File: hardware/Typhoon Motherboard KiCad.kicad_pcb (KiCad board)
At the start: 2 copper layers, 8 parts, among them J1 Conn_01x04_Pin, J2 Conn_02x03_Odd_Even, U1 ESP32-S3-WROOM-1, U2 AZ1117-3.3

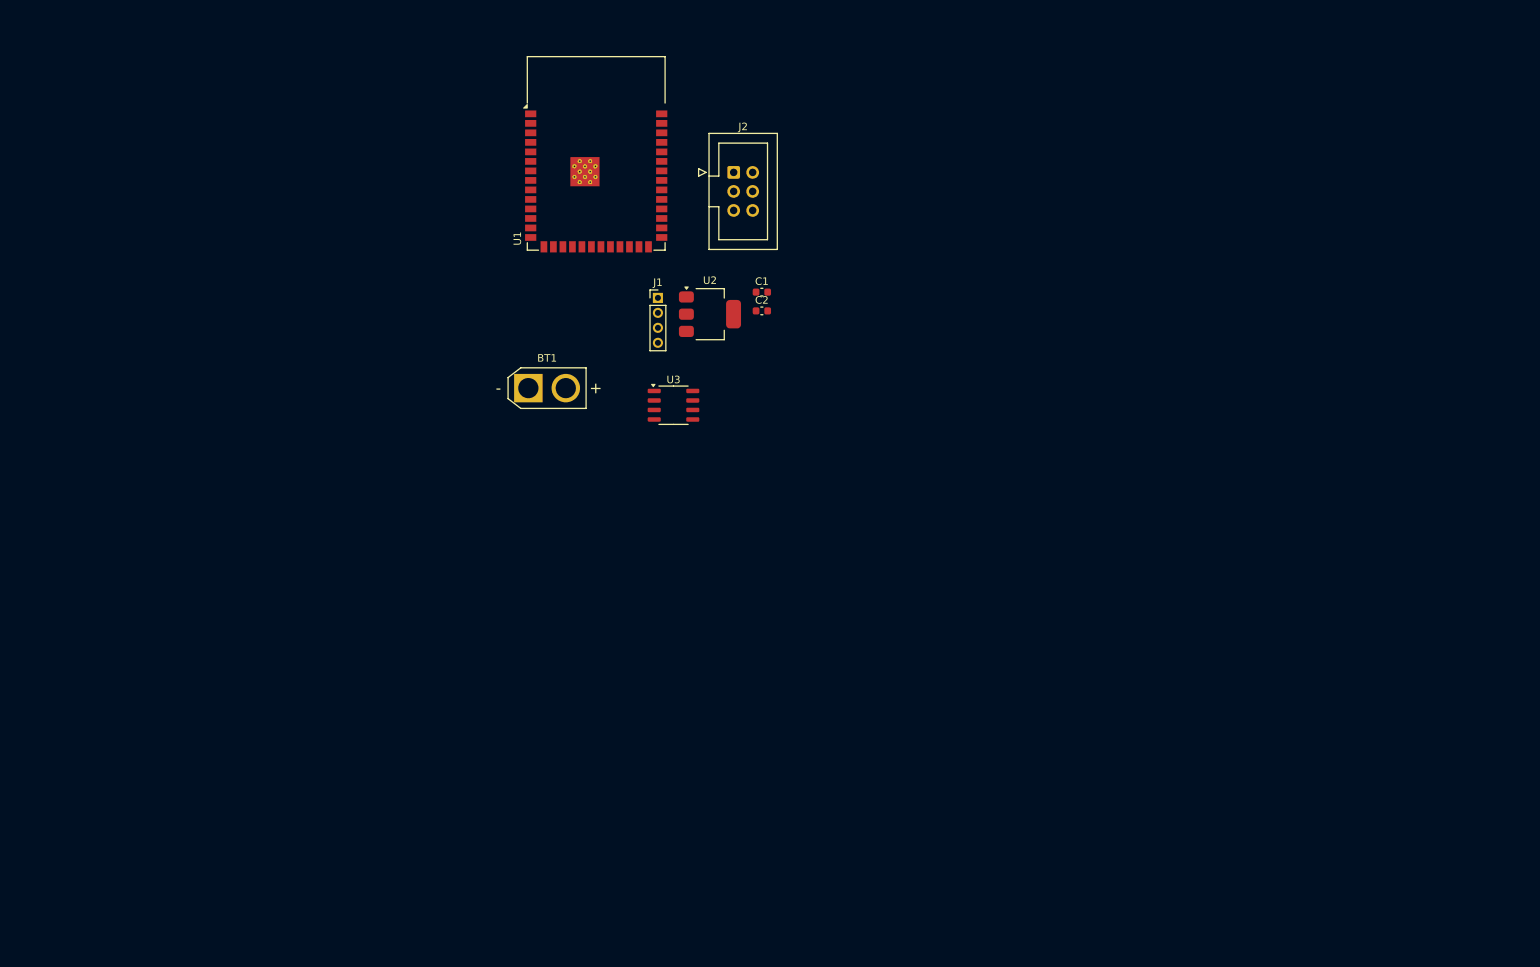
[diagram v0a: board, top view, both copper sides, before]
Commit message: Update Schematics and Start PCB
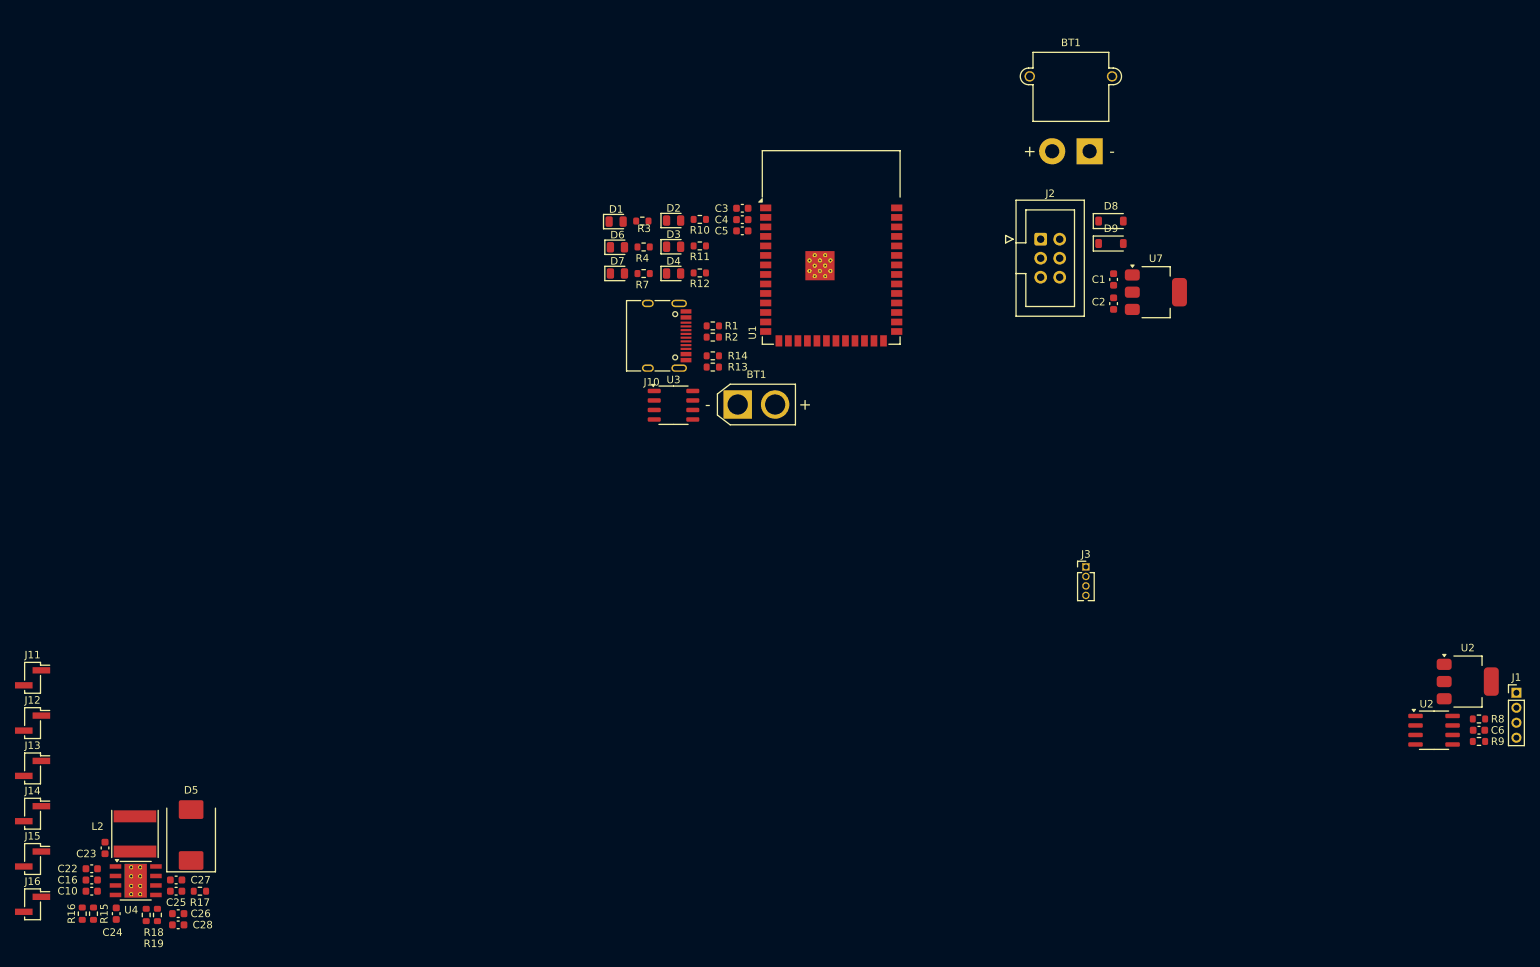
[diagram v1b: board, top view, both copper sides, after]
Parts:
- added BT1: XT30, Connector_AMASS:AMASS_XT30PW-M_1x02_P2.50mm_Horizontal, F.Cu at (176.0, 73.2)
- added C10: 4.7u, Capacitor_SMD:C_0603_1608Metric, F.Cu at (42.7, 172.0)
- added C16: 4.7u, Capacitor_SMD:C_0603_1608Metric, F.Cu at (42.7, 170.5)
- added C22: 4.7u, Capacitor_SMD:C_0603_1608Metric, F.Cu at (42.7, 169.0)
- added C23: 0.1u, Capacitor_SMD:C_0603_1608Metric, F.Cu at (44.5, 166.2)
- added C24: 0.01u, Capacitor_SMD:C_0603_1608Metric, F.Cu at (46.0, 175.0)
- added C25: 1000p, Capacitor_SMD:C_0603_1608Metric, F.Cu at (54.0, 172.0)
- added C26: 47u, Capacitor_SMD:C_0603_1608Metric, F.Cu at (54.3, 175.0)
- added C27: 47u, Capacitor_SMD:C_0603_1608Metric, F.Cu at (54.0, 170.5)
- added C28: 47u, Capacitor_SMD:C_0603_1608Metric, F.Cu at (54.3, 176.5)
- added C3: 10u, Capacitor_SMD:C_0603_1608Metric, F.Cu at (129.6, 80.8)
- added C4: 1u, Capacitor_SMD:C_0603_1608Metric, F.Cu at (129.6, 82.3)
- added C5: 0.1u, Capacitor_SMD:C_0603_1608Metric, F.Cu at (129.6, 83.8)
- added C6: 4.7n, Capacitor_SMD:C_0603_1608Metric, F.Cu at (228.0, 150.5)
- added D1: LED, LED_SMD:LED_0805_2012Metric, F.Cu at (112.8, 82.6)
- added D2: LED, LED_SMD:LED_0805_2012Metric, F.Cu at (120.4, 82.4)
- added D3: LED, LED_SMD:LED_0805_2012Metric, F.Cu at (120.4, 85.9)
- added D4: LED, LED_SMD:LED_0805_2012Metric, F.Cu at (120.4, 89.5)
- added D5: B340, Diode_SMD:D_SMC, F.Cu at (56.0, 164.5)
- added D6: LED, LED_SMD:LED_0805_2012Metric, F.Cu at (112.9, 86.0)
- added D7: LED, LED_SMD:LED_0805_2012Metric, F.Cu at (112.9, 89.5)
- added D8: D, Diode_SMD:D_SOD-123, F.Cu at (178.8, 82.5)
- added D9: D, Diode_SMD:D_SOD-123, F.Cu at (178.8, 85.5)
- added J10: USB_C_Receptacle_USB2.0, Connector_USB:USB_C_Receptacle_HRO_TYPE-C-31-M-12, F.Cu at (118.0, 97.8)
- added J11: Conn_01x02_Pin, Connector_PinHeader_2.00mm:PinHeader_1x02_P2.00mm_Vertical_SMD_Pin1Right, F.Cu at (34.8, 143.5)
- added J12: Conn_01x02_Pin, Connector_PinHeader_2.00mm:PinHeader_1x02_P2.00mm_Vertical_SMD_Pin1Right, F.Cu at (34.8, 149.6)
- added J13: Conn_01x02_Pin, Connector_PinHeader_2.00mm:PinHeader_1x02_P2.00mm_Vertical_SMD_Pin1Right, F.Cu at (34.8, 155.6)
- added J14: Conn_01x02_Pin, Connector_PinHeader_2.00mm:PinHeader_1x02_P2.00mm_Vertical_SMD_Pin1Right, F.Cu at (34.8, 161.7)
- added J15: Conn_01x02_Pin, Connector_PinHeader_2.00mm:PinHeader_1x02_P2.00mm_Vertical_SMD_Pin1Right, F.Cu at (34.8, 167.7)
- added J16: Conn_01x02_Pin, Connector_PinHeader_2.00mm:PinHeader_1x02_P2.00mm_Vertical_SMD_Pin1Right, F.Cu at (34.8, 173.8)
- added J3: Conn_01x04_Pin, Connector_PinHeader_1.27mm:PinHeader_1x04_P1.27mm_Vertical, F.Cu at (175.5, 128.7)
- added L2: 4.7u, Inductor_SMD:L_Taiyo-Yuden_NR-60xx, F.Cu at (48.5, 164.3)
- added R1: 22R, Resistor_SMD:R_0603_1608Metric, F.Cu at (125.7, 96.5)
- added R10: 320, Resistor_SMD:R_0603_1608Metric, F.Cu at (123.9, 82.3)
- added R11: 320, Resistor_SMD:R_0603_1608Metric, F.Cu at (123.9, 85.8)
- added R12: 320, Resistor_SMD:R_0603_1608Metric, F.Cu at (123.9, 89.4)
- added R13: 5.1K, Resistor_SMD:R_0603_1608Metric, F.Cu at (125.7, 102.0)
- added R14: 5.1K, Resistor_SMD:R_0603_1608Metric, F.Cu at (125.7, 100.5)
- added R15: 200k, Resistor_SMD:R_0603_1608Metric, F.Cu at (43.0, 175.0)
- added R16: 98k, Resistor_SMD:R_0603_1608Metric, F.Cu at (41.5, 175.0)
- added R17: 29.4k, Resistor_SMD:R_0603_1608Metric, F.Cu at (57.2, 172.0)
- added R18: 10.2k, Resistor_SMD:R_0603_1608Metric, F.Cu at (50.0, 175.2)
- added R19: 3.24k, Resistor_SMD:R_0603_1608Metric, F.Cu at (51.5, 175.2)
- added R2: 22R, Resistor_SMD:R_0603_1608Metric, F.Cu at (125.7, 98.0)
- added R3: 320, Resistor_SMD:R_0603_1608Metric, F.Cu at (116.3, 82.5)
- added R4: 320, Resistor_SMD:R_0603_1608Metric, F.Cu at (116.4, 86.0)
- added R7: 320, Resistor_SMD:R_0603_1608Metric, F.Cu at (116.4, 89.5)
- added R8: 60, Resistor_SMD:R_0603_1608Metric, F.Cu at (228.0, 149.0)
- added R9: 60, Resistor_SMD:R_0603_1608Metric, F.Cu at (228.0, 152.0)
- added U2: SN65HVD233, Package_SO:SOIC-8_3.9x4.9mm_P1.27mm, F.Cu at (222.0, 150.5)
- added U4: TPS54331DDA, Package_SO:TI_SO-PowerPAD-8_ThermalVias, F.Cu at (48.6, 170.6)
- added U7: MCP1825S, Package_TO_SOT_SMD:SOT-223-3_TabPin2, F.Cu at (184.8, 92.0)
- moved J1 126.2 mm to (233.0, 145.5)
- moved U2 112.5 mm to (226.5, 144.0)
- moved C1 47.0 mm to (179.2, 90.3), turned to 90 degrees
- moved C2 47.0 mm to (179.2, 93.5), turned to -90 degrees
- moved J2 42.0 mm to (169.5, 84.9)
- moved U1 33.8 mm to (141.5, 86.0)
- moved BT1 28.0 mm to (129.0, 107.0)
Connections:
- J1 pad 1: +3V3 -> GND
- J1 pad 2: GND -> +3.3V
- J1 pad 3: /CANH -> /CAN_{H}
- J1 pad 4: /CANL -> /CAN_{L}
- J2 pad 2: +3V3 -> +3.3V
- J2 pad 3: /TX -> /Prog/TypeC_{TX}
- J2 pad 5: /RX -> /Prog/TypeC_{RX}
- U1 pad 10: unconnected-(U1-IO17-Pad10) -> /Mother_{TX}
- U1 pad 11: unconnected-(U1-IO18-Pad11) -> /Mother_{RX}
- U1 pad 12: unconnected-(U1-IO8-Pad12) -> /LED_{4}
- U1 pad 13: Net-(U1-IO19) -> /D-
- U1 pad 14: Net-(U1-IO20) -> /D+
- U1 pad 2: +3V3 -> +3.3V
- U1 pad 36: /RX -> /Prog/TypeC_{RX}
- U1 pad 37: /TX -> /Prog/TypeC_{TX}
- U1 pad 5: unconnected-(U1-IO5-Pad5) -> /LED_{1}
- U1 pad 6: unconnected-(U1-IO6-Pad6) -> /LED_{2}
- U1 pad 7: unconnected-(U1-IO7-Pad7) -> /LED_{3}
- U1 pad 8: unconnected-(U1-IO15-Pad8) -> /LED_{5}
- U1 pad 9: unconnected-(U1-IO16-Pad9) -> /LED_{6}

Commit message: First draft of PCB
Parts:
- removed the BT1 at (129.0, 107.0)
- removed the U2 at (226.5, 144.0)
- removed the U2 at (222.0, 150.5)
- removed U3: ~, Package_SO:SO-8_3.9x4.9mm_P1.27mm
- added U2: SN65HVD233, Package_SO:SOIC-8_3.9x4.9mm_P1.27mm, F.Cu at (157.5, 103.6)
- moved J16 133.1 mm to (157.2, 121.3), turned to 90 degrees
- moved J15 125.2 mm to (151.2, 121.3), turned to 90 degrees
- moved C23 122.5 mm to (154.5, 112.2)
- moved L2 121.4 mm to (159.0, 114.0)
- moved D5 120.9 mm to (166.0, 114.5)
- moved J14 117.4 mm to (145.1, 121.3), turned to 90 degrees
- moved R17 114.1 mm to (150.7, 106.7)
- moved R18 114.1 mm to (143.5, 109.8)
- moved R19 114.1 mm to (145.0, 109.8)
- moved C10 114.1 mm to (136.3, 106.7)
- moved C16 114.1 mm to (136.3, 105.2)
- moved C22 114.1 mm to (136.3, 103.7)
- moved C24 114.1 mm to (139.5, 109.7)
- moved C25 114.1 mm to (147.5, 106.7)
- moved C26 114.1 mm to (147.8, 109.7)
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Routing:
- net +3.3V: track 0.00 -> 74.7 mm, vias 0 -> 3
- net /Prog/TypeC_{RX}: track 0.00 -> 57.1 mm
- net +5V: track 0.00 -> 37.6 mm
- net /EN: track 0.00 -> 33.5 mm, vias 0 -> 1
- net /Prog/TypeC_{TX}: track 0.00 -> 32.3 mm
- net /LED_{6}: track 0.00 -> 30.5 mm, vias 0 -> 2
- net /LED_{5}: track 0.00 -> 29.6 mm, vias 0 -> 2
- net /LED_{4}: track 0.00 -> 29.1 mm, vias 0 -> 2
- net Net-(D5-K): track 0.00 -> 29.1 mm, vias 0 -> 2
- net +BATT: track 0.00 -> 28.8 mm
- net VDC: track 0.00 -> 28.1 mm
- net /LED_{3}: track 0.00 -> 27.5 mm, vias 0 -> 2
- net /LED_{2}: track 0.00 -> 26.9 mm, vias 0 -> 2
- net /Mother_{RX}: track 0.00 -> 26.2 mm
- net /LED_{1}: track 0.00 -> 26.2 mm, vias 0 -> 2
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- added copper zone on F.Cu, net +3.3V
- added copper zone on F.Cu, net +3.3VA
- added copper zone on B.Cu, net GND
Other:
- board outline added: 67.5 x 73 mm

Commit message: Finalized First Draft of the PCB
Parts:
- moved U2 0.60 mm to (158.0, 103.8)
- turned D8 to 180 degrees
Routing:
- net Net-(J10-CC1): track 12.4 -> 8.34 mm, vias 0 -> 2
- net +3.3V: track 74.7 -> 78.7 mm
- net /Prog/TypeC_{RX}: track 57.1 -> 54.8 mm
- net Net-(D2-A): track 0.00 -> 1.80 mm
- net Net-(D3-A): track 0.00 -> 1.78 mm
- net Net-(D4-A): track 0.00 -> 1.77 mm
- net Net-(D1-A): track 0.00 -> 1.77 mm
- net Net-(D6-A): track 0.00 -> 1.75 mm
- net Net-(D7-A): track 0.00 -> 1.74 mm
- net +5V: track 37.6 -> 39.3 mm
- net /D-: track 24.9 -> 26.6 mm
- net /D+: track 24.0 -> 25.7 mm
- net +BATT: track 28.8 -> 30.4 mm
- net /Prog/TypeC_{TX}: track 32.3 -> 33.7 mm
- net GND: vias 37 -> 39

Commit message: Fixed Placement issues (aesthetic fixes)
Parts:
- moved J3 47.3 mm to (112.7, 120.2), turned to 90 degrees
- moved J10 0.93 mm to (112.0, 85.2)
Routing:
- net +3.3V: track 78.7 -> 141.7 mm
- net /Mother_{TX}: track 26.0 -> 38.9 mm, vias 0 -> 2
- net /Mother_{RX}: track 26.2 -> 38.0 mm, vias 0 -> 2
- net /D+: track 25.7 -> 24.8 mm
- net Net-(J10-CC1): track 8.34 -> 9.06 mm
- net VDC: track 28.1 -> 27.6 mm

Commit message: Update (Round Edges)
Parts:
- moved J11 0.65 mm to (127.0, 120.7)
- moved J12 0.65 mm to (133.0, 120.7)
- moved J13 0.65 mm to (139.1, 120.7)
- moved J14 0.65 mm to (145.1, 120.7)
- moved J15 0.65 mm to (151.2, 120.7)
- moved J16 0.65 mm to (157.2, 120.7)
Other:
- board size 67.5 x 73 mm -> 65.7 x 44.9 mm
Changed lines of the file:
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@@
 		(tags "usb usb-c 2.0 pd")
 		(property "Reference" "J10"
-			(at -6.82 1.05 180)
+			(at -0.75 4.8 -90)
 			(layer "F.SilkS")
 			(effects
@@
 	(footprint "Connector_PinHeader_2.00mm:PinHeader_1x02_P2.00mm_Vertical_SMD_Pin1Right"
 		(layer "F.Cu")
-		(at 133 121.325 90)
+		(at 133 120.675 90)
 		(descr "surface-mounted straight pin header, 1x02, 2.00mm pitch, single row, style 2 (pin 1 right)")
 		(tags "Surface mounted pin header SMD 1x02 2.00mm single row style2 pin1 right")
 		(property "Reference" "J12"
-			(at 0 -3.06 270)
+			(at -2.075 -1 0)
 			(layer "F.SilkS")
 			(effects
@@
 	(footprint "Connector_PinHeader_2.00mm:PinHeader_1x02_P2.00mm_Vertical_SMD_Pin1Right"
 		(layer "F.Cu")
-		(at 126.95 121.325 90)
+		(at 126.95 120.675 90)
 		(descr "surface-mounted straight pin header, 1x02, 2.00mm pitch, single row, style 2 (pin 1 right)")
 		(tags "Surface mounted pin header SMD 1x02 2.00mm single row style2 pin1 right")
 		(property "Reference" "J11"
-			(at 0 -3.06 270)
+			(at -2.075 -0.95 0)
 			(layer "F.SilkS")
 			(effects
@@
 	(footprint "Connector_PinHeader_2.00mm:PinHeader_1x02_P2.00mm_Vertical_SMD_Pin1Right"
 		(layer "F.Cu")
-		(at 157.2 121.325 90)
+		(at 157.2 120.675 90)
 		(descr "surface-mounted straight pin header, 1x02, 2.00mm pitch, single row, style 2 (pin 1 right)")
 		(tags "Surface mounted pin header SMD 1x02 2.00mm single row style2 pin1 right")
 		(property "Reference" "J16"
-			(at 0 -3.06 270)
+			(at -2.075 -0.95 0)
 			(layer "F.SilkS")
 			(effects
@@
 	(footprint "Connector_PinHeader_2.00mm:PinHeader_1x02_P2.00mm_Vertical_SMD_Pin1Right"
 		(layer "F.Cu")
-		(at 151.15 121.325 90)
+		(at 151.15 120.675 90)
 		(descr "surface-mounted straight pin header, 1x02, 2.00mm pitch, single row, style 2 (pin 1 right)")
 		(tags "Surface mounted pin header SMD 1x02 2.00mm single row style2 pin1 right")
 		(property "Reference" "J15"
-			(at 0 -3.06 270)
+			(at -2.075 -0.9 0)
 			(layer "F.SilkS")
 			(effects
@@
 	(footprint "Connector_PinHeader_2.00mm:PinHeader_1x02_P2.00mm_Vertical_SMD_Pin1Right"
 		(layer "F.Cu")
-		(at 145.1 121.325 90)
+		(at 145.1 120.675 90)
 		(descr "surface-mounted straight pin header, 1x02, 2.00mm pitch, single row, style 2 (pin 1 right)")
 		(tags "Surface mounted pin header SMD 1x02 2.00mm single row style2 pin1 right")
 		(property "Reference" "J14"
-			(at 0 -3.06 270)
+			(at -2.075 -0.85 0)
 			(layer "F.SilkS")
 			(effects
@@
 	(footprint "Connector_PinHeader_2.00mm:PinHeader_1x02_P2.00mm_Vertical_SMD_Pin1Right"
 		(layer "F.Cu")
-		(at 139.05 121.325 90)
+		(at 139.05 120.675 90)
 		(descr "surface-mounted straight pin header, 1x02, 2.00mm pitch, single row, style 2 (pin 1 right)")
 		(tags "Surface mounted pin header SMD 1x02 2.00mm single row style2 pin1 right")
 		(property "Reference" "J13"
-			(at 0 -3.06 270)
+			(at -2.075 -0.8 0)
 			(layer "F.SilkS")
 			(effects
@@
 	)
 	(gr_line
-		(start 173 128)
-		(end 173 55)
+		(start 171.25 123)
+		(end 171.18934 81.06066)
 		(stroke
 			(width 0.05)
@@
 	)
 	(gr_line
-		(start 105.5 55)
-		(end 105.5 128)
+		(start 105.56066 81.06066)
+		(end 105.56066 122.93934)
+		(stroke
+			(width 0.05)
+			(type default)
+		)
+		(layer "Edge.Cuts")
+	)
+	(gr_arc
+		(start 171.25 123)
+		(mid 170.81066 124.06066)
+		(end 169.75 124.5)
+		(stroke
+			(width 0.05)
+			(type default)
+		)
+		(layer "Edge.Cuts")
+	)
+	(gr_arc
+		(start 169.68934 79.56066)
+		(mid 170.75 80)
+		(end 171.18934 81.06066)
 		(stroke
 			(width 0.05)
@@
 	)
 	(gr_line
-		(start 105.5 128)
-		(end 173 128)
+		(start 107.06066 124.43934)
+		(end 169.75 124.5)
 		(stroke
 			(width 0.05)
@@
 	)
 	(gr_line
-		(start 173 55)
-		(end 105.5 55)
+		(start 169.68934 79.56066)
+		(end 107.06066 79.56066)
+		(stroke
+			(width 0.05)
+			(type default)
+		)
+		(layer "Edge.Cuts")
+	)
+	(gr_arc
+		(start 105.56066 81.06066)
+		(mid 106 80)
+		(end 107.06066 79.56066)
+		(stroke
+			(width 0.05)
+			(type default)
+		)
+		(layer "Edge.Cuts")
+	)
+	(gr_arc
+		(start 107.06066 124.43934)
+		(mid 106 124)
+		(end 105.56066 122.93934)
 		(stroke
 			(width 0.05)
@@
 		(polygon
 			(pts
-				(xy 106.25 79.5) (xy 106 113) (xy 131 113) (xy 131 102) (xy 153.5 102) (xy 153.5 107.5) (xy 172 107.5)
-				(xy 172 80) (xy 117 79.5) (xy 117.25 79.5)
+				(xy 104.75 79.25) (xy 104.5 113) (xy 131 113) (xy 131 102) (xy 153.5 102) (xy 153.5 107.5) (xy 172 107.5)
+				(xy 172 79.25) (xy 117.485 78.5) (xy 117.25 79.25)
 			)
 		)
@@
 		(polygon
 			(pts
-				(xy 116.75 79.5) (xy 117 79.5) (xy 172 80) (xy 172 127) (xy 106 127) (xy 106 79.5) (xy 106.75 79.5)
+				(xy 116.75 78.5) (xy 117 78.5) (xy 173.25 78.25) (xy 173.25 126.75) (xy 104 126.75) (xy 104 78.25)
+				(xy 106.75 78.5)
 			)
 		)
